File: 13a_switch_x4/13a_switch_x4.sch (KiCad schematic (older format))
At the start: 21 parts, among them P1 CONN_01X01, P2 CONN_01X01, P3 CONN_01X05, P4 CONN_01X01, P5 CONN_01X01, P6 CONN_01X01, P7 CONN_01X01, P8 CONN_01X01, Q1 Q_NMOS_GDSD, Q2 Q_NMOS_GDSD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

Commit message: inputs rev1, 13a_switch_x4 rev1
both hardware and firmware is working
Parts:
- C1: DIGIKEY 445-13057-1-ND -> 478-5230-1-ND
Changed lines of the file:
@@
 F 1 "10uF" H 4125 1450 50  0000 L CNN
 F 2 "Capacitors_SMD:C_1210_HandSoldering" H 4138 1400 50  0001 C CNN
-F 3 "http://www.digikey.com/product-detail/en/tdk-corporation/CGA6P3X8R1C106M250AB/445-13057-1-ND/3954723" H 4100 1550 50  0001 C CNN
-F 4 "445-13057-1-ND" H 4100 1550 60  0001 C CNN "DIGIKEY"
+F 3 "http://datasheets.avx.com/TPS.pdf" H 4100 1550 50  0001 C CNN
+F 4 "478-5230-1-ND" H 4100 1550 60  0001 C CNN "DIGIKEY"
 	1    4100 1550
 	1    0    0    -1

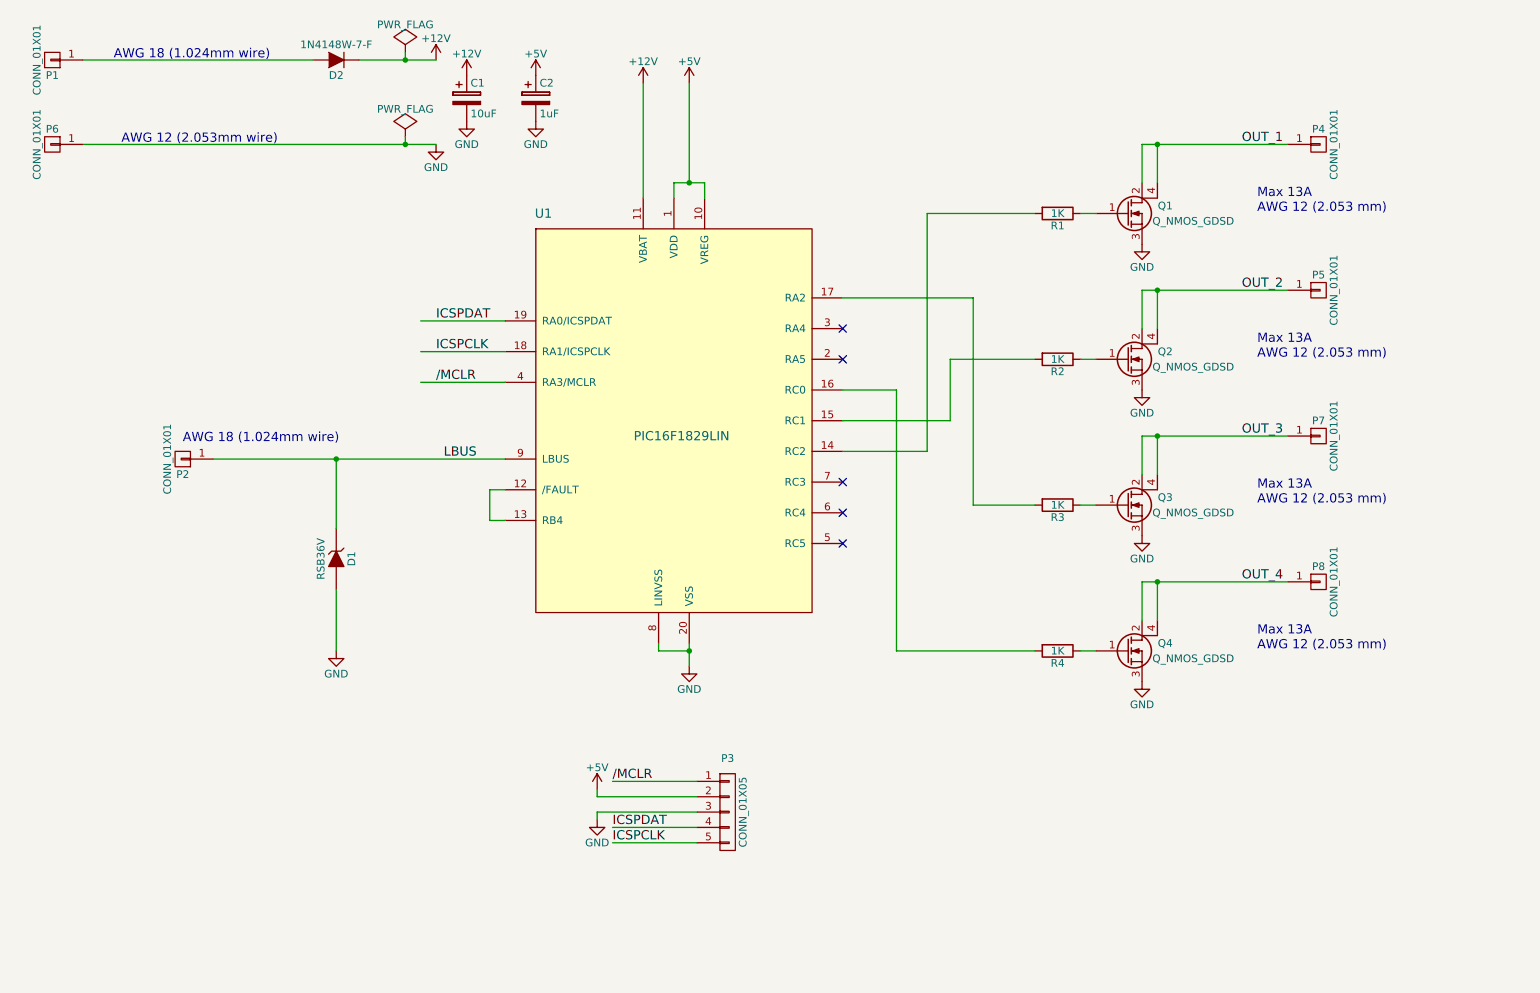
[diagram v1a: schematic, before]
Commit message: 13a_switch rev2
- daisy-chain connector
- adding a DIP switch to select the LIN device
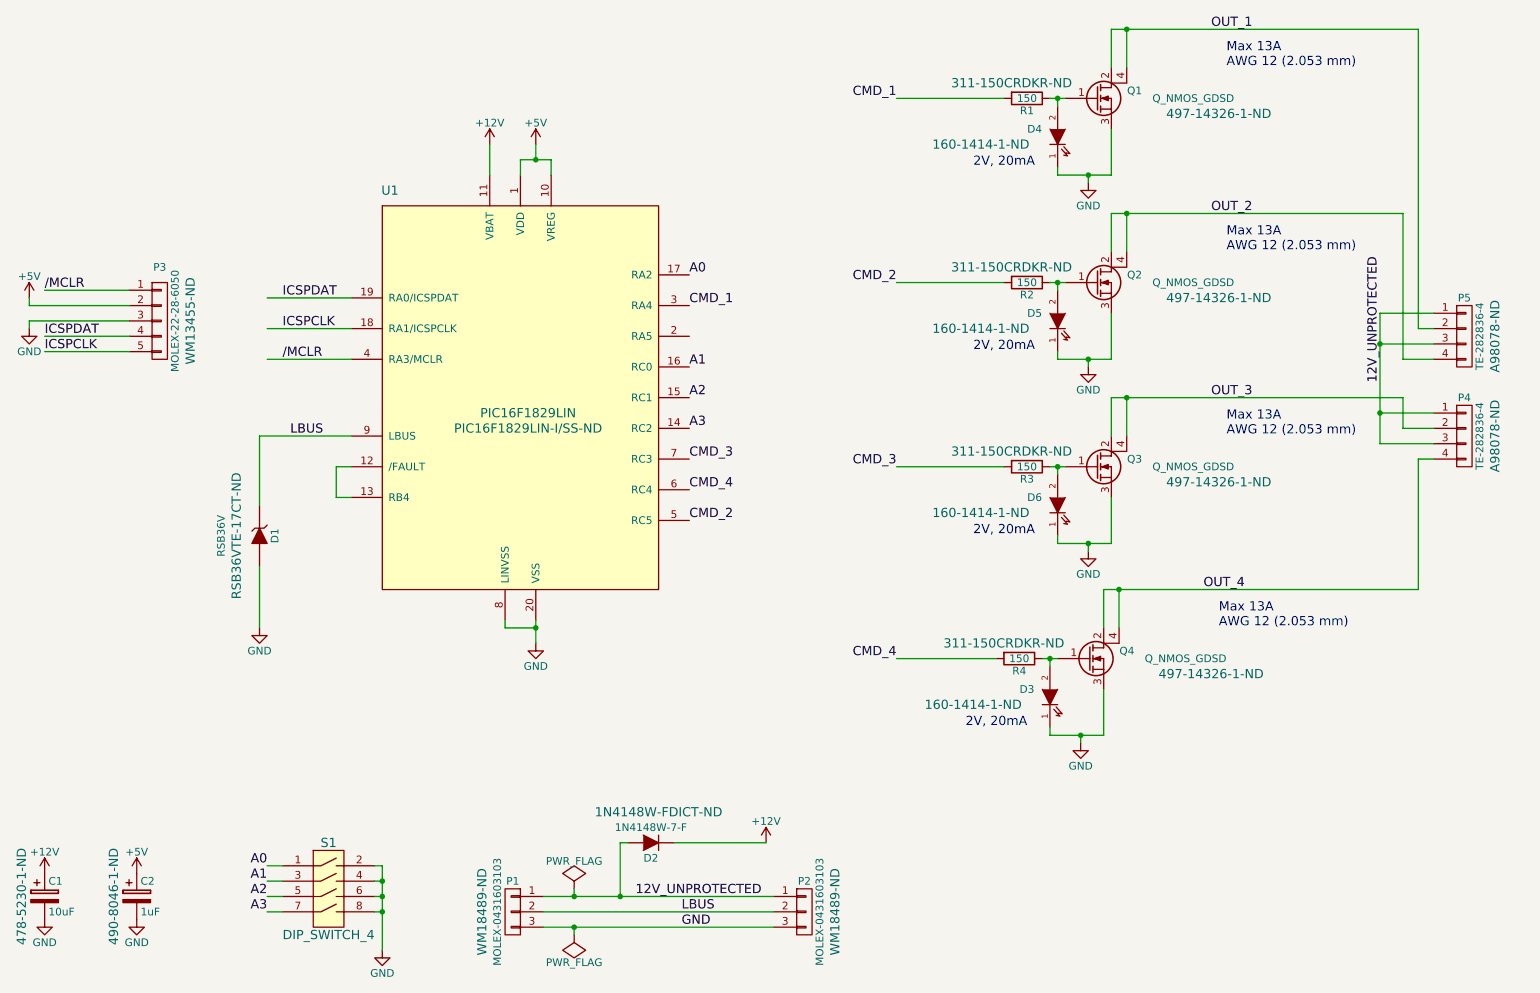
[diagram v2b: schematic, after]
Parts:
- removed P1, P2, P4, P5, P6, P7, P8: CONN_01X01, Connect:1pin, symbol CONN_01X01
- added D3, D4, D5, D6: LITEON-LTST-C170KGKT, LEDs:LED_0805, symbol LED
- added P1, P2: MOLEX-0431603103, Connectors_Molex:Molex_Sabre_43160-XX03_03x7.49mm_Angled_BoardLock, symbol CONN_01X03
- added P4, P5: TE-282836-4, Connect:bornier4, symbol CONN_01X04
- added S1: DIP_SWITCH_4, footprints:Copal_CHS-04TB, symbol DIP_SWITCH_4
- P3: value CONN_01X05 -> MOLEX-22-28-6050; DIGIKEY (none) -> WM13455-ND
- R1, R2, R3, R4: value 1K -> 150; DIGIKEY 311-1.00KCRCT-ND -> 311-150CRDKR-ND
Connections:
- net labels added: 12V_UNPROTECTED, A0, A1, A2, A3, CMD_1, CMD_2, CMD_3, CMD_4
- wire segments 61 -> 98
- no-connect marks 5 -> 0
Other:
- note added: "2V, 20mA"
- note removed: "AWG 12 (2.053mm wire)"
- note removed: "AWG 18 (1.024mm wire)"
- moved on the sheet: C1, C2, D1, D2, P3, Q1, Q2, Q3, Q4, R4, U1

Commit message: minor updates (DigiKey PN, cleaning)
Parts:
- R1, R2, R3, R4: DIGIKEY 311-150CRDKR-ND -> 311-150CRCT-ND
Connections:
- no-connect marks 0 -> 1
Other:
- note added: "AWG 16"
- note removed: "Max 13A\nAWG 12 (2.053 mm)"
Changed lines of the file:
@@
 $EndComp
 $Comp
-L +12V #PWR9
+L +12V #PWR01
 U 1 1 57DF768A
 P 4250 1850
-F 0 "#PWR9" H 4250 1700 50  0001 C CNN
+F 0 "#PWR01" H 4250 1700 50  0001 C CNN
 F 1 "+12V" H 4250 1990 50  0000 C CNN
 F 2 "" H 4250 1850 50  0000 C CNN
@@
 $EndComp
 $Comp
-L GND #PWR14
+L GND #PWR02
 U 1 1 57DF7E85
 P 8150 2100
-F 0 "#PWR14" H 8150 1850 50  0001 C CNN
+F 0 "#PWR02" H 8150 1850 50  0001 C CNN
 F 1 "GND" H 8150 1950 50  0000 C CNN
 F 2 "" H 8150 2100 50  0000 C CNN
@@
 $EndComp
 $Comp
-L GND #PWR11
+L GND #PWR03
 U 1 1 57DFB653
 P 4550 5100
-F 0 "#PWR11" H 4550 4850 50  0001 C CNN
+F 0 "#PWR03" H 4550 4850 50  0001 C CNN
 F 1 "GND" H 4550 4950 50  0000 C CNN
 F 2 "" H 4550 5100 50  0000 C CNN
@@
 $EndComp
 $Comp
-L +12V #PWR12
+L +12V #PWR04
 U 1 1 57DFC07F
-P 6050 6400
-F 0 "#PWR12" H 6050 6250 50  0001 C CNN
-F 1 "+12V" H 6050 6540 50  0000 C CNN
-F 2 "" H 6050 6400 50  0000 C CNN
-F 3 "" H 6050 6400 50  0000 C CNN
-	1    6050 6400
-	1    0    0    -1
-$EndComp
-$Comp
-L +5V #PWR10
+P 6250 6400
+F 0 "#PWR04" H 6250 6250 50  0001 C CNN
+F 1 "+12V" H 6250 6540 50  0000 C CNN
+F 2 "" H 6250 6400 50  0000 C CNN
+F 3 "" H 6250 6400 50  0000 C CNN
+	1    6250 6400
+	1    0    0    -1
+$EndComp
+$Comp
+L +5V #PWR05
 U 1 1 57DFC341
 P 4550 1850
-F 0 "#PWR10" H 4550 1700 50  0001 C CNN
+F 0 "#PWR05" H 4550 1700 50  0001 C CNN
 F 1 "+5V" H 4550 1990 50  0000 C CNN
 F 2 "" H 4550 1850 50  0000 C CNN
@@
 $EndComp
 $Comp
-L GND #PWR4
+L GND #PWR06
 U 1 1 57DFC522
 P 1350 6900
-F 0 "#PWR4" H 1350 6650 50  0001 C CNN
+F 0 "#PWR06" H 1350 6650 50  0001 C CNN
 F 1 "GND" H 1350 6750 50  0000 C CNN
 F 2 "" H 1350 6900 50  0000 C CNN
@@
 $EndComp
 $Comp
-L +12V #PWR3
+L +12V #PWR07
 U 1 1 57DFC55A
 P 1350 6600
-F 0 "#PWR3" H 1350 6450 50  0001 C CNN
+F 0 "#PWR07" H 1350 6450 50  0001 C CNN
 F 1 "+12V" H 1350 6740 50  0000 C CNN
 F 2 "" H 1350 6600 50  0000 C CNN
@@
 $EndComp
 $Comp
-L +5V #PWR5
+L +5V #PWR08
 U 1 1 57DFC6C4
 P 1950 6600
-F 0 "#PWR5" H 1950 6450 50  0001 C CNN
+F 0 "#PWR08" H 1950 6450 50  0001 C CNN
 F 1 "+5V" H 1950 6740 50  0000 C CNN
 F 2 "" H 1950 6600 50  0000 C CNN
@@
 $EndComp
 $Comp
-L GND #PWR6
+L GND #PWR09
 U 1 1 57DFC6FC
 P 1950 6900
-F 0 "#PWR6" H 1950 6650 50  0001 C CNN
+F 0 "#PWR09" H 1950 6650 50  0001 C CNN
 F 1 "GND" H 1950 6750 50  0000 C CNN
 F 2 "" H 1950 6900 50  0000 C CNN
@@
 /MCLR
 $Comp
-L +5V #PWR1
+L +5V #PWR010
 U 1 1 57E0B6A0
 P 1250 2850
-F 0 "#PWR1" H 1250 2700 50  0001 C CNN
+F 0 "#PWR010" H 1250 2700 50  0001 C CNN
 F 1 "+5V" H 1250 2990 50  0000 C CNN
 F 2 "" H 1250 2850 50  0000 C CNN
@@
 $EndComp
 $Comp
-L GND #PWR2
+L GND #PWR011
 U 1 1 57E0BA65
 P 1250 3050
-F 0 "#PWR2" H 1250 2800 50  0001 C CNN
+F 0 "#PWR011" H 1250 2800 50  0001 C CNN
 F 1 "GND" H 1250 2900 50  0000 C CNN
 F 2 "" H 1250 3050 50  0000 C CNN
@@
 Wire Wire Line
 	2750 4600 2750 5000
-Text Notes 9050 1350 0    60   ~ 0
-Max 13A\nAWG 12 (2.053 mm)
-$Comp
-L GND #PWR7
+$Comp
+L GND #PWR012
 U 1 1 57E227B3
 P 2750 5000
-F 0 "#PWR7" H 2750 4750 50  0001 C CNN
+F 0 "#PWR012" H 2750 4750 50  0001 C CNN
 F 1 "GND" H 2750 4850 50  0000 C CNN
 F 2 "" H 2750 5000 50  0000 C CNN
@@
 $EndComp
 $Comp
-L GND #PWR15
+L GND #PWR013
 U 1 1 57FC7617
 P 8150 3300
-F 0 "#PWR15" H 8150 3050 50  0001 C CNN
+F 0 "#PWR013" H 8150 3050 50  0001 C CNN
 F 1 "GND" H 8150 3150 50  0000 C CNN
 F 2 "" H 8150 3300 50  0000 C CNN
@@
 Wire Wire Line
 	8300 2550 8300 2300
-Text Notes 9050 2550 0    60   ~ 0
-Max 13A\nAWG 12 (2.053 mm)
+Text Notes 10600 2750 0    60   ~ 0
+AWG 16
 $Comp
 L Q_NMOS_GDSD Q3
@@
 $EndComp
 $Comp
-L GND #PWR16
+L GND #PWR014
 U 1 1 57FC7897
 P 8150 4500
-F 0 "#PWR16" H 8150 4250 50  0001 C CNN
+F 0 "#PWR014" H 8150 4250 50  0001 C CNN
 F 1 "GND" H 8150 4350 50  0000 C CNN
 F 2 "" H 8150 4500 50  0000 C CNN
@@
 Wire Wire Line
 	8300 3750 8300 3500
-Text Notes 9050 3750 0    60   ~ 0
-Max 13A\nAWG 12 (2.053 mm)
 $Comp
 L Q_NMOS_GDSD Q4
@@
 $EndComp
 $Comp
-L GND #PWR13
+L GND #PWR015
 U 1 1 57FC7992
 P 8100 5750
-F 0 "#PWR13" H 8100 5500 50  0001 C CNN
+F 0 "#PWR015" H 8100 5500 50  0001 C CNN
 F 1 "GND" H 8100 5600 50  0000 C CNN
 F 2 "" H 8100 5750 50  0000 C CNN
@@
 U 1 1 57FC799F
 P 7700 5200
-F 0 "R4" V 7780 5200 50  0000 C CNN
+F 0 "R4" V 7500 5200 50  0000 C CNN
 F 1 "150" V 7700 5200 50  0000 C CNN
 F 2 "Resistors_SMD:R_0805_HandSoldering" V 7630 5200 50  0001 C CNN
 F 3 "" H 7700 5200 50  0001 C CNN
-F 4 "311-150CRDKR-ND" V 7600 5100 60  0000 C CNN "DIGIKEY"
+F 4 "311-150CRCT-ND" V 7600 5100 60  0000 C CNN "DIGIKEY"
 	1    7700 5200
 	0    1    1    0
@@
 Wire Wire Line
 	8250 5000 8250 4750
-Text Notes 9000 5000 0    60   ~ 0
-Max 13A\nAWG 12 (2.053 mm)
 Wire Wire Line
 	7600 1550 6900 1550
@@
 	7600 2750 6900 2750
 Wire Wire Line
-	5450 6400 6050 6400
+	5450 6400 6250 6400
 Wire Wire Line
 	7600 3950 6900 3950
@@
 	7550 5200 6900 5200
 $Comp
-L PWR_FLAG #FLG2
+L PWR_FLAG #FLG016
 U 1 1 57FD97C2
 P 4800 7000
-F 0 "#FLG2" H 4800 7095 50  0001 C CNN
+F 0 "#FLG016" H 4800 7095 50  0001 C CNN
 F 1 "PWR_FLAG" H 4800 7180 50  0000 C CNN
 F 2 "" H 4800 7000 50  0000 C CNN
@@
 $EndComp
 $Comp
-L PWR_FLAG #FLG1
+L PWR_FLAG #FLG017
 U 1 1 57FD9AE5
-P 4800 6700
-F 0 "#FLG1" H 4800 6795 50  0001 C CNN
-F 1 "PWR_FLAG" H 4800 6880 50  0000 C CNN
-F 2 "" H 4800 6700 50  0000 C CNN
-F 3 "" H 4800 6700 50  0000 C CNN
-	1    4800 6700
+P 6000 6300
+F 0 "#FLG017" H 6000 6395 50  0001 C CNN
+F 1 "PWR_FLAG" H 6000 6480 50  0000 C CNN
+F 2 "" H 6000 6300 50  0000 C CNN
+F 3 "" H 6000 6300 50  0000 C CNN
+	1    6000 6300
 	1    0    0    -1
 $EndComp
@@
 LBUS
 Wire Wire Line
-	4800 6700 4800 6750
-Connection ~ 4800 6750
-Wire Wire Line
 	4800 7000 4800 6950
 Connection ~ 4800 6950
@@
 U 1 1 58428698
 P 7750 3950
-F 0 "R3" V 7830 3950 50  0000 C CNN
+F 0 "R3" V 7550 3950 50  0000 C CNN
 F 1 "150" V 7750 3950 50  0000 C CNN
 F 2 "Resistors_SMD:R_0805_HandSoldering" V 7680 3950 50  0001 C CNN
 F 3 "" H 7750 3950 50  0001 C CNN
-F 4 "311-150CRDKR-ND" V 7650 3850 60  0000 C CNN "DIGIKEY"
+F 4 "311-150CRCT-ND" V 7650 3850 60  0000 C CNN "DIGIKEY"
 	1    7750 3950
 	0    1    1    0
@@
 U 1 1 584289A7
 P 7750 2750
-F 0 "R2" V 7830 2750 50  0000 C CNN
+F 0 "R2" V 7550 2750 50  0000 C CNN
 F 1 "150" V 7750 2750 50  0000 C CNN
 F 2 "Resistors_SMD:R_0805_HandSoldering" V 7680 2750 50  0001 C CNN
 F 3 "" H 7750 2750 50  0001 C CNN
-F 4 "311-150CRDKR-ND" V 7650 2650 60  0000 C CNN "DIGIKEY"
+F 4 "311-150CRCT-ND" V 7650 2650 60  0000 C CNN "DIGIKEY"
 	1    7750 2750
 	0    1    1    0
@@
 U 1 1 58428BB2
 P 7750 1550
-F 0 "R1" V 7830 1550 50  0000 C CNN
+F 0 "R1" V 7550 1550 50  0000 C CNN
 F 1 "150" V 7750 1550 50  0000 C CNN
 F 2 "Resistors_SMD:R_0805_HandSoldering" V 7680 1550 50  0001 C CNN
 F 3 "" H 7750 1550 50  0001 C CNN
-F 4 "311-150CRDKR-ND" V 7650 1450 60  0000 C CNN "DIGIKEY"
+F 4 "311-150CRCT-ND" V 7650 1450 60  0000 C CNN "DIGIKEY"
 	1    7750 1550
 	0    1    1    0
@@
 12V_UNPROTECTED
 $Comp
-L GND #PWR8
+L GND #PWR018
 U 1 1 584497B3
 P 3550 7100
-F 0 "#PWR8" H 3550 6850 50  0001 C CNN
+F 0 "#PWR018" H 3550 6850 50  0001 C CNN
 F 1 "GND" H 3550 6950 50  0000 C CNN
 F 2 "" H 3550 7100 50  0000 C CNN
@@
 F 2 "footprints:Copal_CHS-04TB" H 3250 7050 60  0001 C CNN
 F 3 "http://www.nidec-copal-electronics.com/e/catalog/switch/chs.pdf" H 3250 7050 60  0001 C CNN
-F 4 "563-1008-1-ND" H 3200 6700 60  0001 C CNN "DIGIKEY"
+F 4 "563-1008-1-ND" H 3200 7100 60  0000 C CNN "DIGIKEY"
 	1    3200 6700
 	1    0    0    -1
@@
 Text Label 5550 4100 0    60   ~ 0
 CMD_4
+NoConn ~ 5550 3100
+Wire Wire Line
+	6000 6300 6000 6400
+Connection ~ 6000 6400
 $EndSCHEMATC
